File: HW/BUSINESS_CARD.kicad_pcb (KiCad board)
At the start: 2 copper layers, 90 x 55 mm, 16 parts

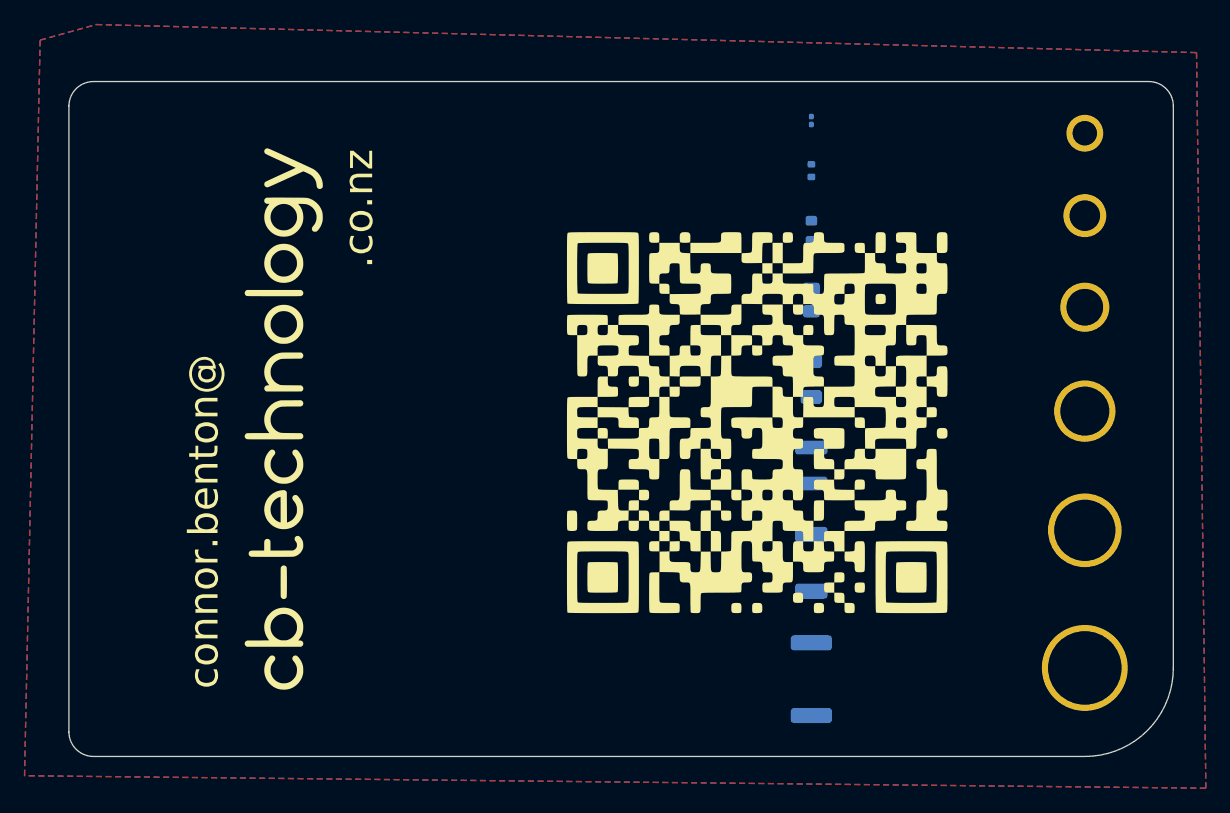
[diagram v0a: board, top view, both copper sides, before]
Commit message: Create Business Card v1.1
Make slightly smaller to fit in wallet
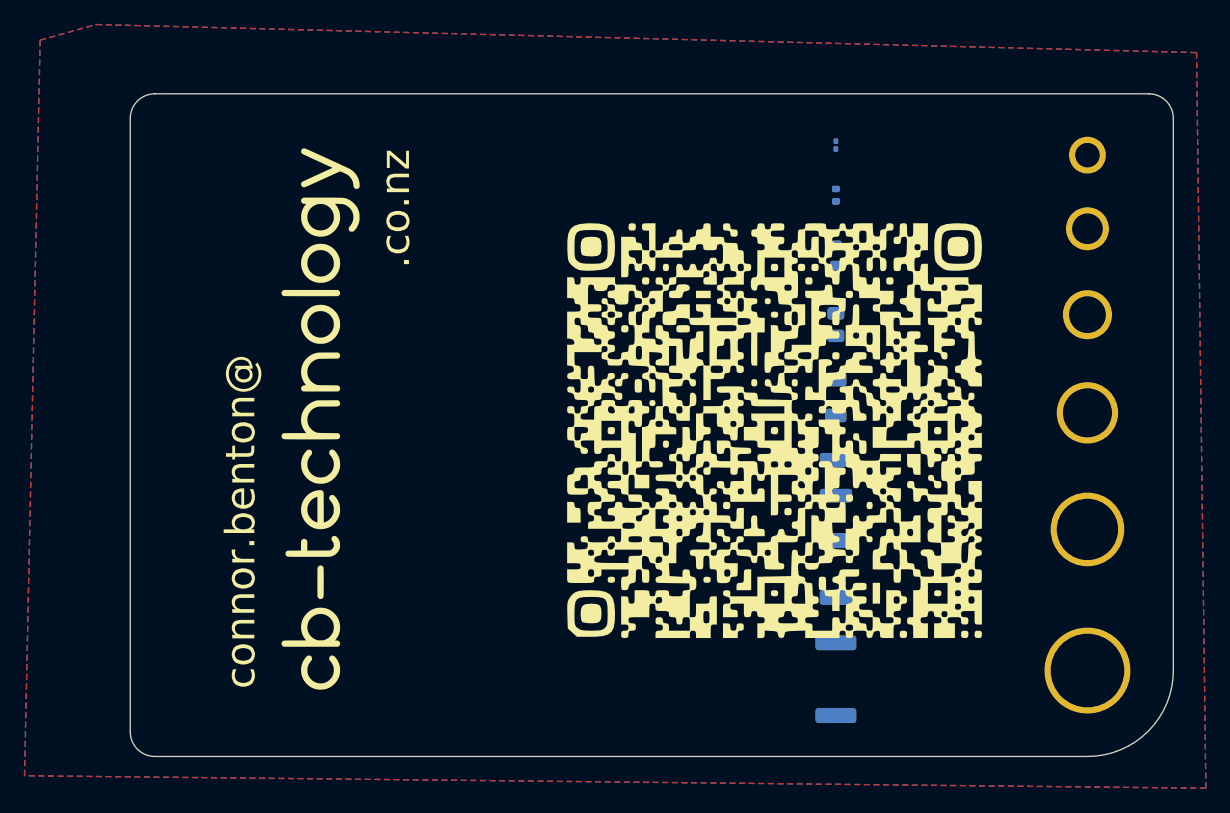
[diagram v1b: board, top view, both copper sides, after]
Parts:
- moved G*** 4.27 mm to (212.5, 151.0), turned to 0 degrees
- moved G*** 3.00 mm to (175.5, 150.0)
- moved R1 2.83 mm to (217.5, 127.7)
- moved R2 2.83 mm to (217.5, 131.8)
- moved R3 2.83 mm to (217.5, 136.7)
- moved R4 2.83 mm to (217.5, 142.3)
- moved R5 2.50 mm to (217.5, 148.2)
- moved R7 2.24 mm to (217.5, 154.8)
- moved R6 2.06 mm to (217.5, 162.2)
- moved R8 2.00 mm to (217.5, 171.2)
- moved H1 1.80 mm to (238.0, 128.5)
- moved H2 1.09 mm to (238.0, 134.5)
- moved H3 0.64 mm to (238.0, 141.5)
- moved H6 0.30 mm to (238.0, 170.5)
- moved H4 0.26 mm to (238.0, 149.5)
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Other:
- board size 90 x 55 mm -> 85 x 54 mm
- board text added: "M2"
- board text added: "M2.5"
- board text added: "M3"
- board text added: "M4"
- board text added: "M5"
- board text added: "M6"
- board text removed: "m2"
- board text removed: "m2.5"
- board text removed: "m3"
- board text removed: "m4"
- board text removed: "m5"
- board text removed: "m6"
